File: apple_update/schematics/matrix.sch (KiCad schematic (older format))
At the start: 210 parts

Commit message: Update labels
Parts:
- gave numbers to parts that had none: 210

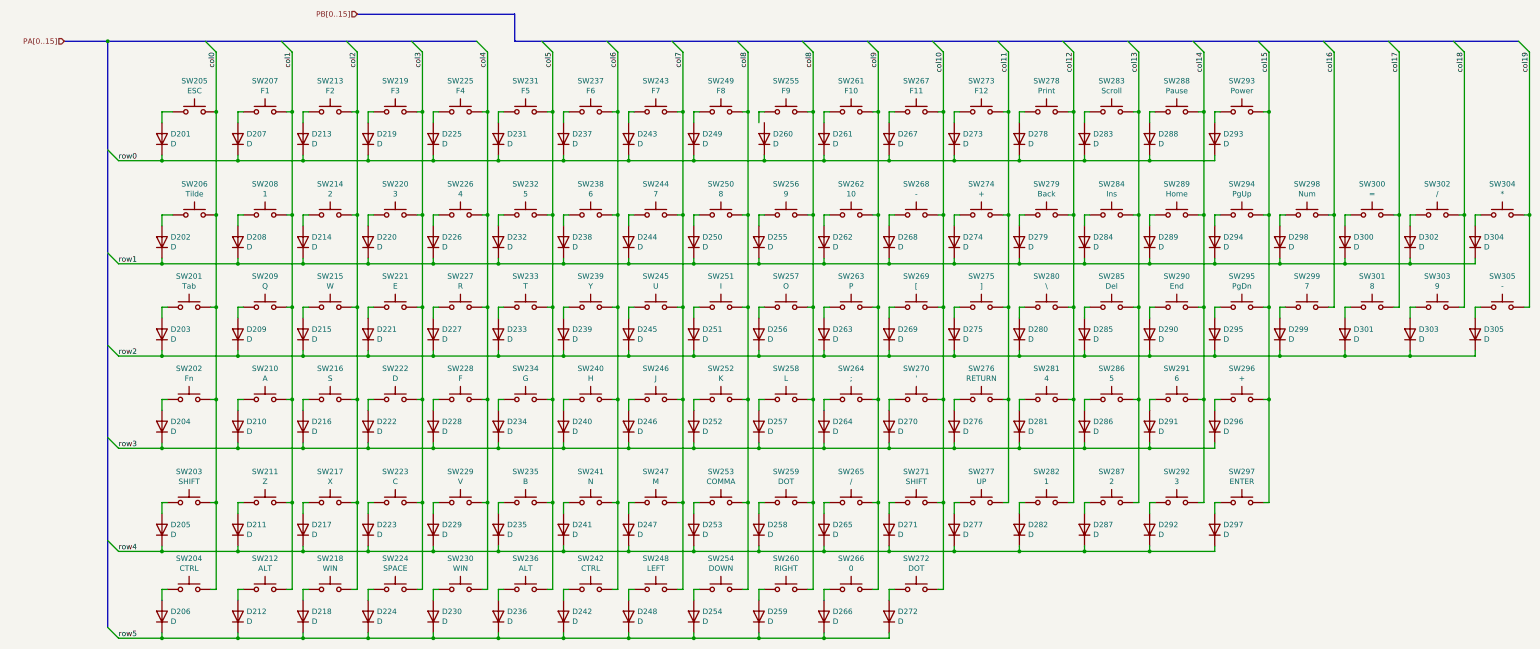
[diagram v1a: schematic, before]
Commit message: updating sch. adding footprint for alps.
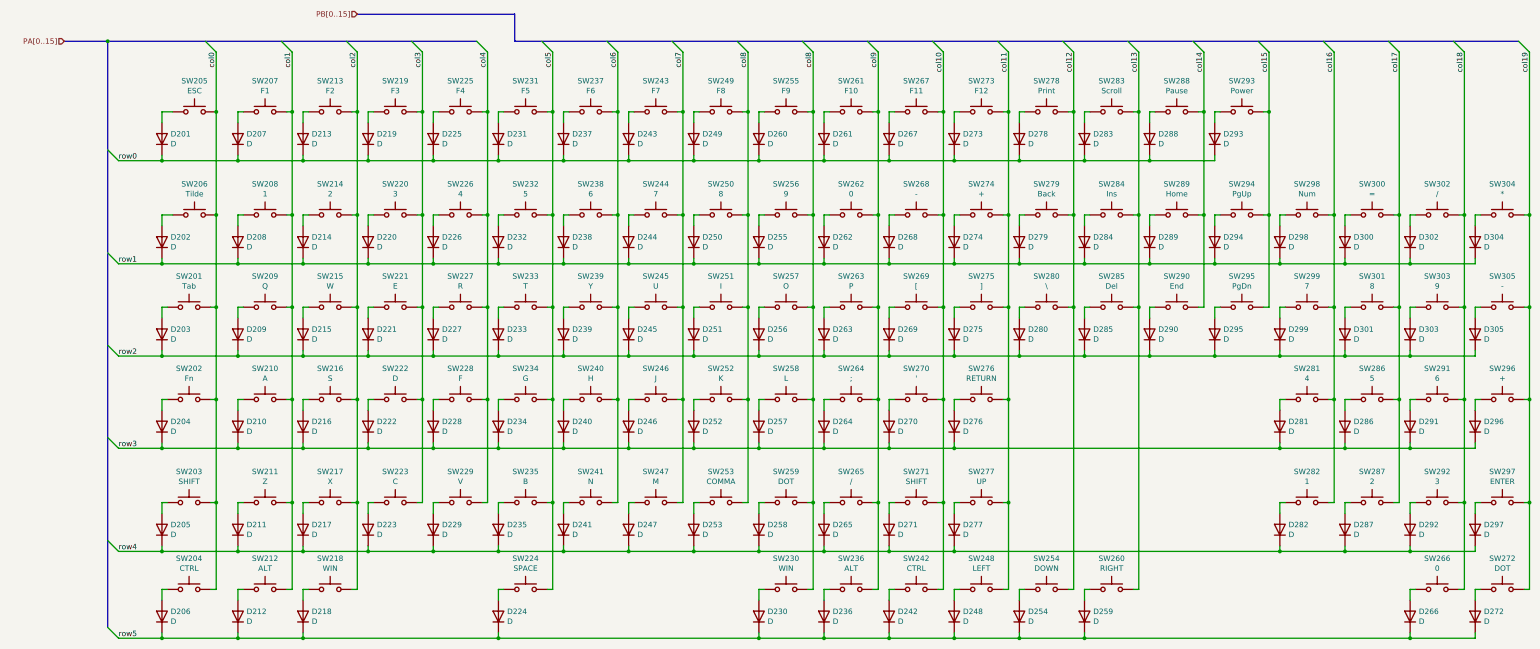
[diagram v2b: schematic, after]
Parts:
- D201, D202, D203, D204, D205, D206, D207, D208, D209, D210, D211, D212, D213, D214, D215, D216, D217, D218, D219, D220, D221, D222, D223, D224, D225, D226, D227, D228, D229, D230, D231, D232, D233, D234, D235, D236, D237, D238, D239, D240, D241, D242, D243, D244, D245, D246, D247, D248, D249, D250, D251, D252, D253, D254, D255, D256, D257, D258, D259, D260, D261, D262, D263, D264, D265, D266, D267, D268, D269, D270, D271, D272, D273, D274, D275, D276, D277, D278, D279, D280, D281, D282, D283, D284, D285, D286, D287, D288, D289, D290, D291, D292, D293, D294, D295, D296, D297, D298, D299, D300, D301, D302, D303, D304, D305: footprint (none) -> Diode_SMD:D_0805_2012Metric_Pad1.15x1.40mm_HandSolder
- SW201, SW202, SW203, SW204, SW205, SW206, SW207, SW208, SW209, SW210, SW211, SW212, SW213, SW214, SW215, SW216, SW217, SW218, SW219, SW220, SW221, SW222, SW223, SW224, SW225, SW226, SW227, SW228, SW229, SW230, SW231, SW232, SW233, SW234, SW235, SW236, SW237, SW238, SW239, SW240, SW241, SW242, SW243, SW244, SW245, SW246, SW247, SW248, SW249, SW250, SW251, SW252, SW253, SW254, SW255, SW256, SW257, SW258, SW259, SW260, SW261, SW263, SW264, SW265, SW266, SW267, SW268, SW269, SW270, SW271, SW272, SW273, SW274, SW275, SW276, SW277, SW278, SW279, SW280, SW281, SW282, SW283, SW284, SW285, SW286, SW287, SW288, SW289, SW290, SW291, SW292, SW293, SW294, SW295, SW296, SW297, SW298, SW299, SW300, SW301, SW302, SW303, SW304, SW305: footprint (none) -> schematics:alps_skcm
- SW262: value 10 -> 0; footprint (none) -> schematics:alps_skcm
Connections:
- net col10: now also SW242.2; no longer SW272.2
- net col11: now also SW248.2
- net col12: now also SW254.2; no longer SW281.2, SW282.2
- net col13: now also SW260.2; no longer SW286.2, SW287.2
- net col14: no longer SW291.2, SW292.2
- net col15: no longer SW296.2, SW297.2
- net col16: now also SW281.2, SW282.2
- net col17: now also SW286.2, SW287.2
- net col18: now also SW266.2, SW291.2, SW292.2
- net col19: now also SW272.2, SW296.2, SW297.2
- net col3: no longer SW224.2
- net col4: no longer SW230.2
- net col5: now also SW224.2; no longer SW236.2
- net col6: no longer SW242.2
- net col7: no longer SW248.2
- net col8: now also SW230.2; no longer SW254.2, SW260.2
- net col9: now also SW236.2; no longer SW266.2
- net at SW255.1: now also D260.2 (A)
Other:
- moved on the sheet: D224, D230, D236, D242, D248, D254, D259, D260, D266, D272, D281, D282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
